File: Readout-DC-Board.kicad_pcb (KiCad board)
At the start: 4 copper layers, 48.3 x 30.5 mm, 11 parts, among them J1 Conn_02x05_Odd_Even, J2 Conn_02x05_Odd_Even, U1 LM2678T-12

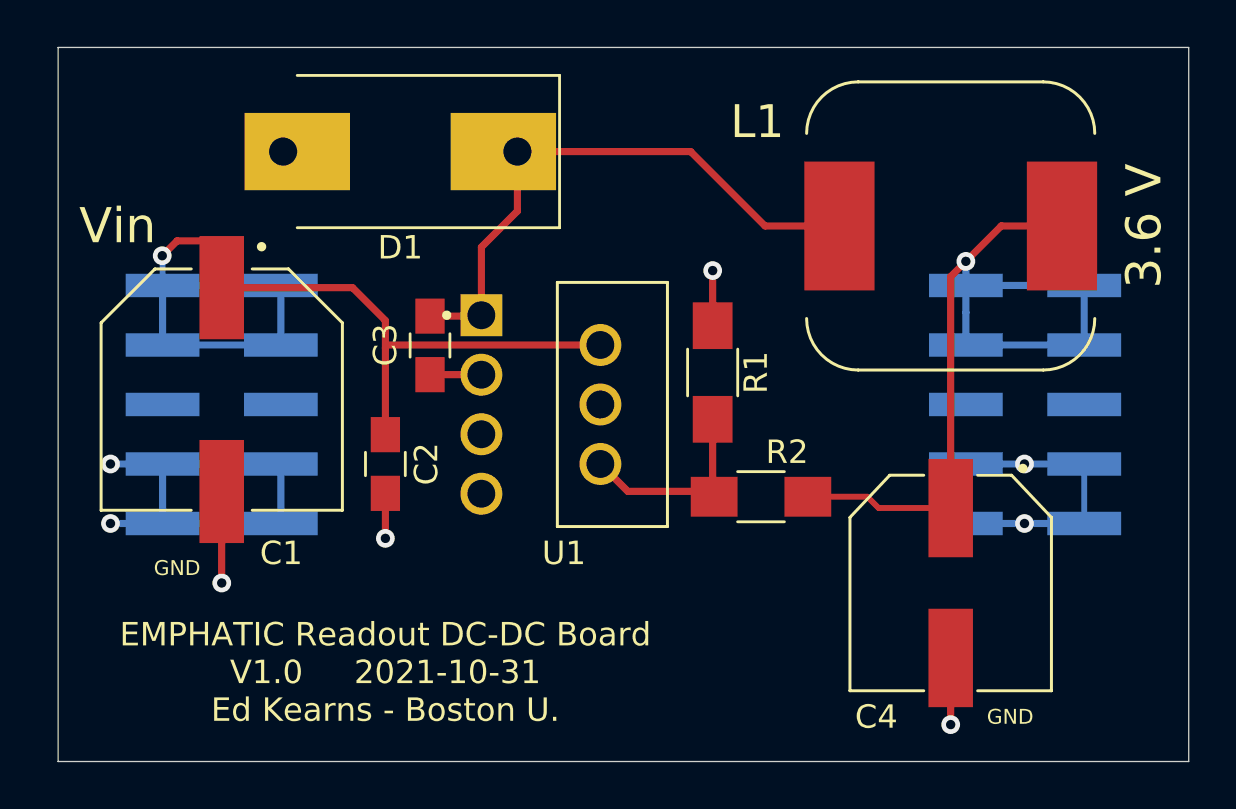
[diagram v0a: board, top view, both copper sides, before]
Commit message: Try again to commit. These are changes suggested by Eric. Rotated regulator.
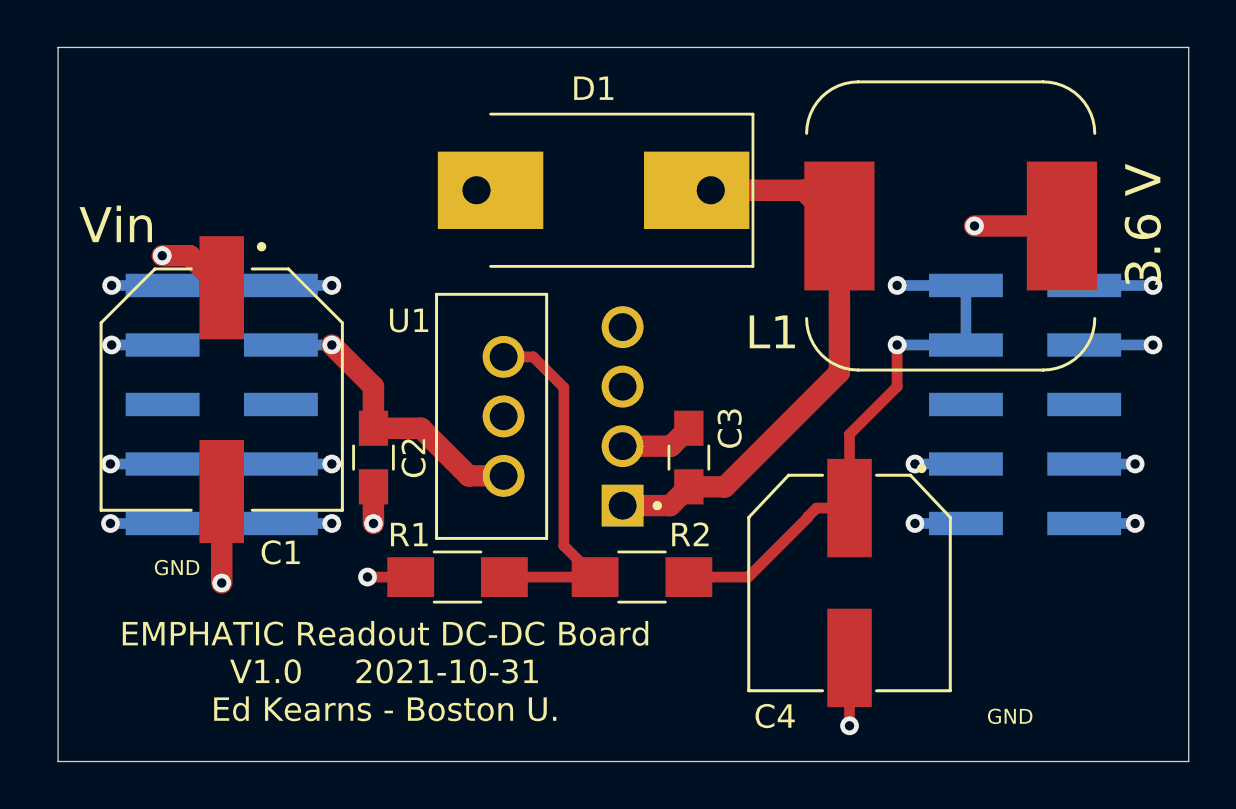
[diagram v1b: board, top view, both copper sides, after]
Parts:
- moved R1 14.0 mm to (93.2, 119.1), turned to 0 degrees
- moved C3 12.0 mm to (103.1, 114.0), turned to 90 degrees
- moved D1 8.42 mm to (99.1, 102.6)
- moved R2 6.13 mm to (101.1, 119.1)
- moved C4 4.32 mm to (110.0, 119.4)
- moved U1 1.14 mm to (96.8, 112.3), turned to 90 degrees
- moved C2 0.58 mm to (89.7, 114.0)
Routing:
- net Net-(C1-Pad1): track 41.6 -> 22.5 mm, vias 1 -> 5
- net GND: track 45.8 -> 27.6 mm, vias 8 -> 12
- net Net-(R1-Pad2): track 8.36 -> 15.6 mm
- net Net-(C4-Pad1): track 39.2 -> 33.9 mm, vias 1 -> 5
- net Net-(C3-Pad2): track 2.19 -> 3.14 mm
- net Net-(C3-Pad1): track 24.9 -> 24.0 mm
- added copper zone on In2.Cu, net Net-(C1-Pad1)
- added copper zone on In2.Cu, net Net-(C4-Pad1)
